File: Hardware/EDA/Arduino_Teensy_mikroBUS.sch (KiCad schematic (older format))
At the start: 30 parts, among them J1 HEADER_F_2.54MM_1R8P_ST_AU_PTH, J2 HEADER_F_2.54MM_1R8P_ST_AU_PTH, J3 HEADER_F_2.54MM_1R14P_ST_AU_P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, J4 HEADER_F_2.54MM_1R14P_ST_AU_P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, J5 Molex_0475710001, M1 FID, M2 FID, M3 FID, P1 HEADER_M_2.54MM_1R4P_ST_AU_PTH, P2 HEADER_M_2.54MM_1R4P_ST_AU_PTH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

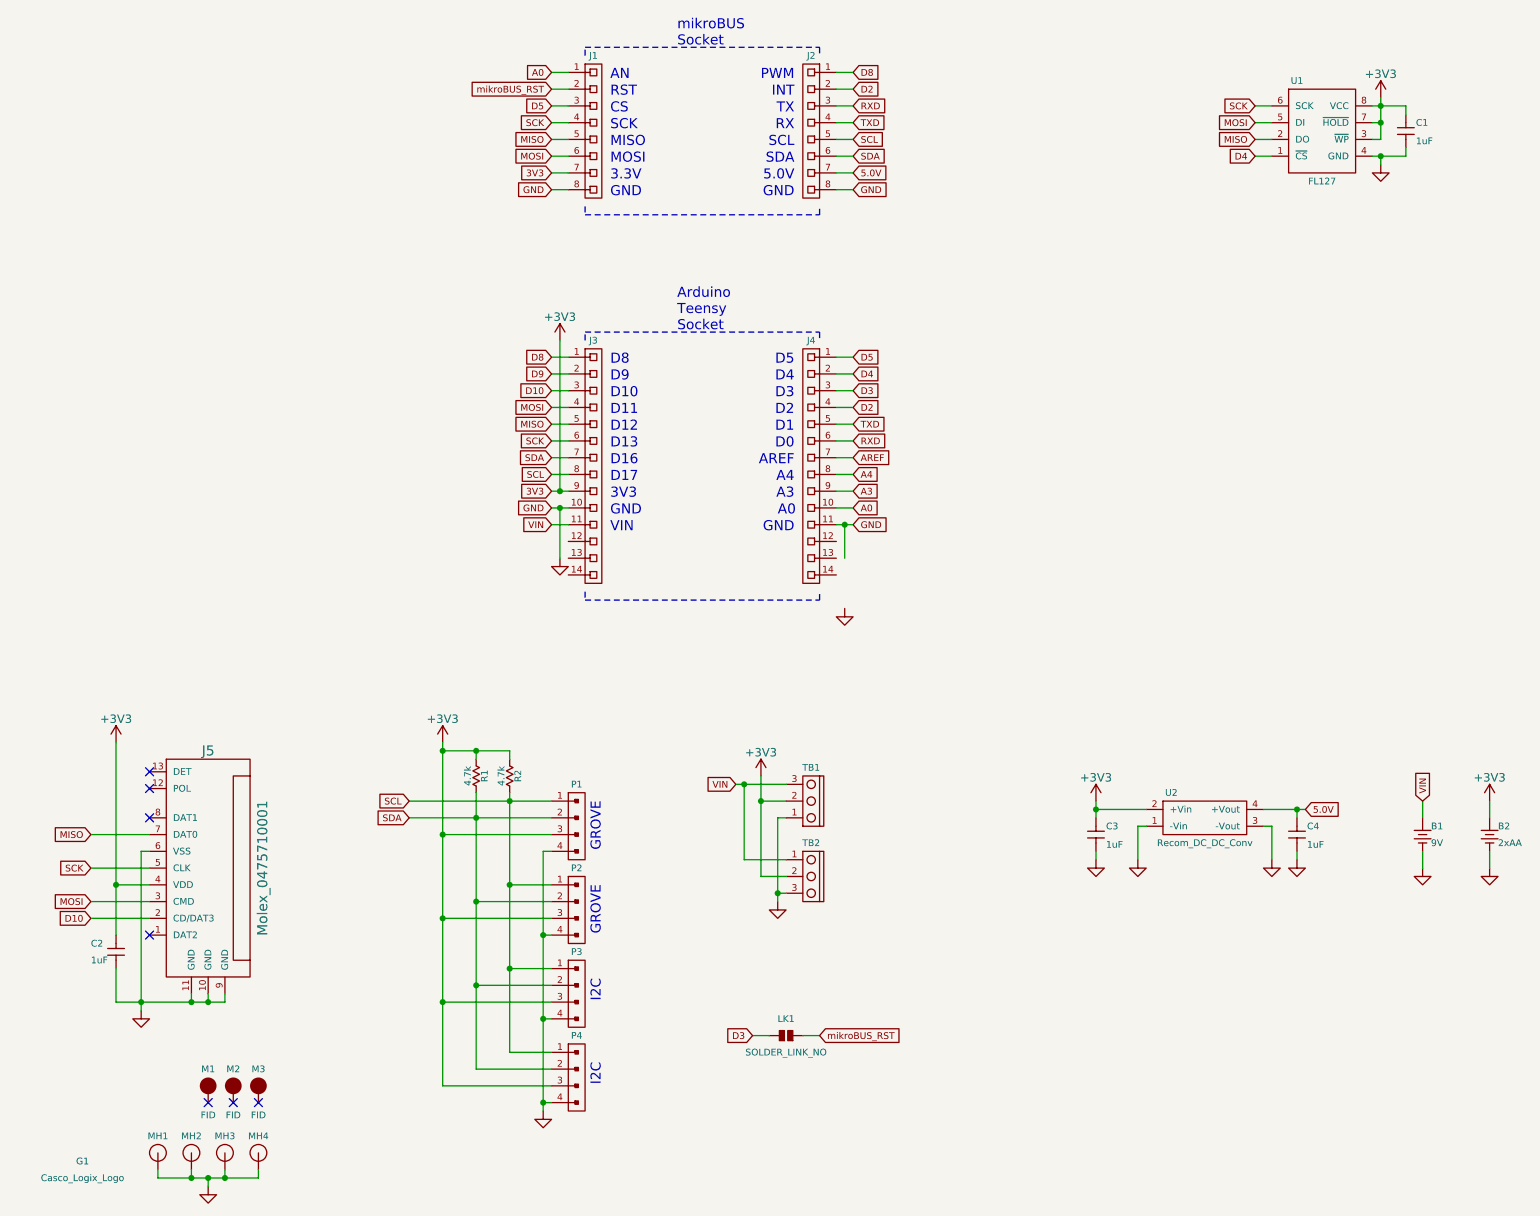
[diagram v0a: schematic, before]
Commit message: Updated schematic, netlist and read in netlist to PCB file.  Added pinouts for Teensy.
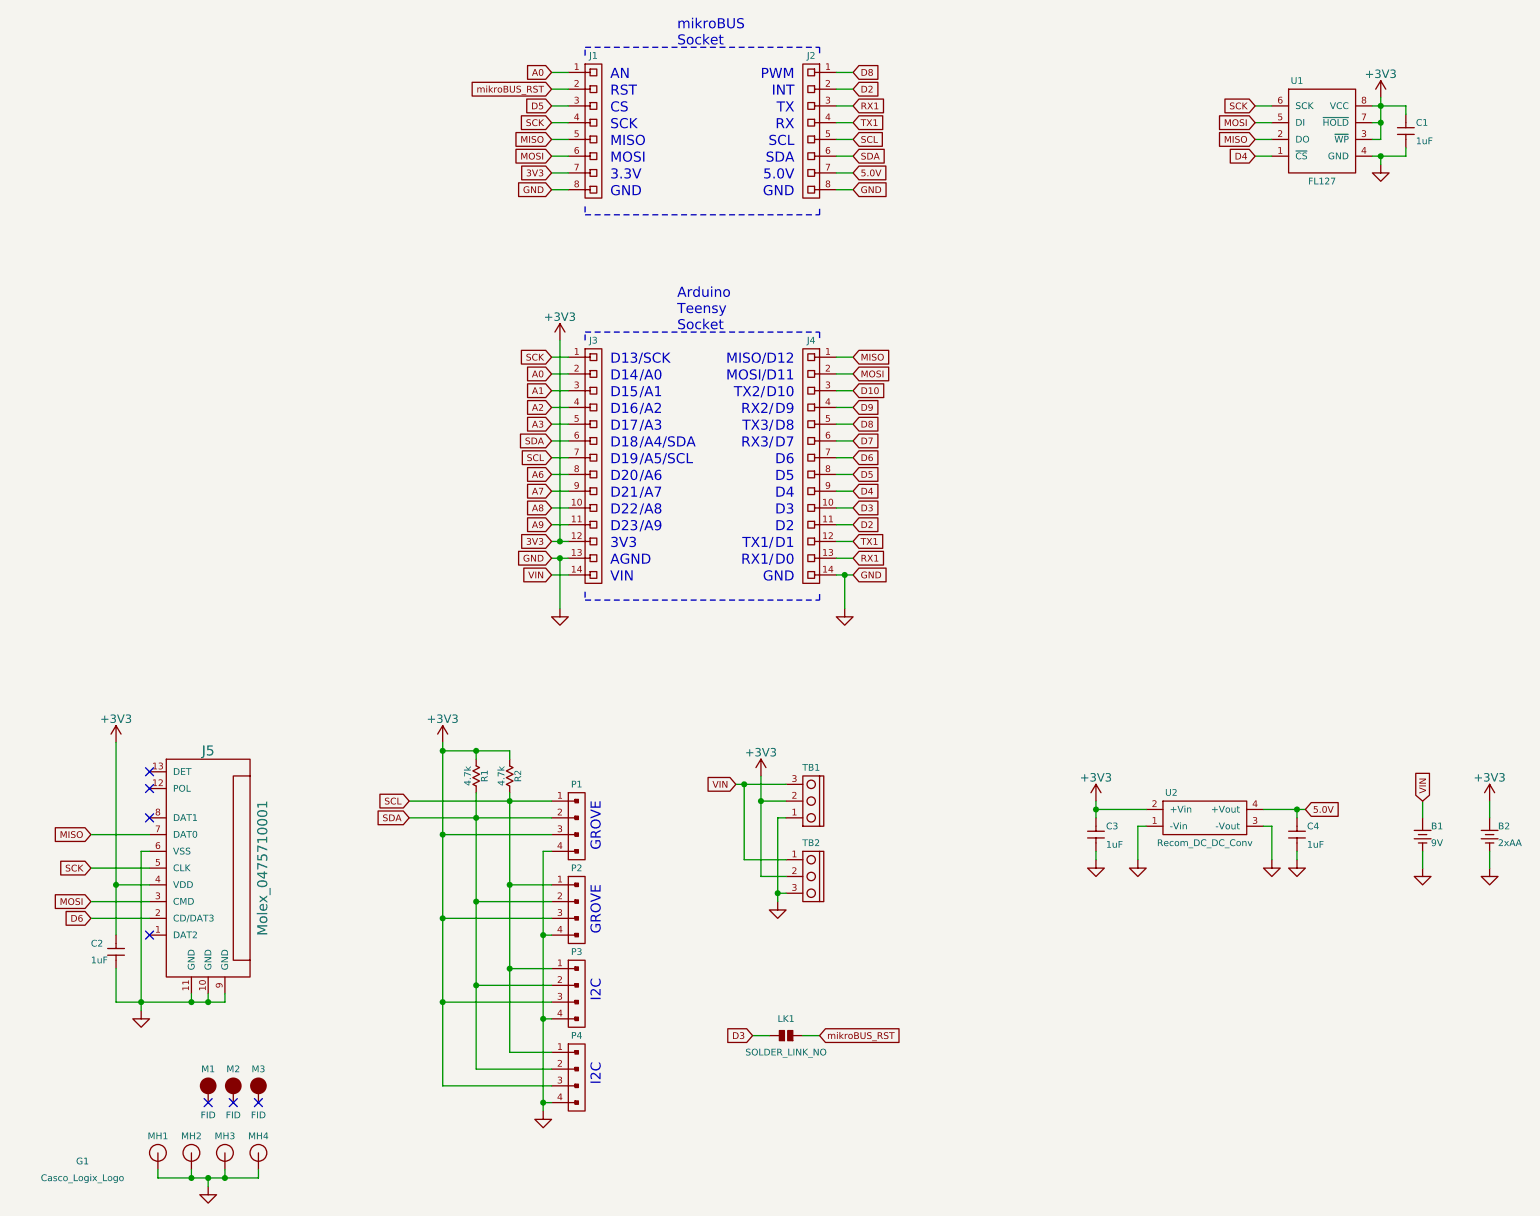
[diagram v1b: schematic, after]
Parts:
- B1: footprint (none) -> Battery:BC9VPC
- B2: footprint (none) -> Battery:Keystone_2462_2AA
- J3, J4: footprint (none) -> Header:HEADER_F_2.54MM_1R14P_ST_AU_PTH
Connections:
- net A4 is gone; now on net D5: J4.8 (P1)
- net +3V3: now also J3.12 (P1); no longer J3.9 (P1)
- net A0: now also J3.2 (P1); no longer J4.10 (P1)
- net A3: now also J3.5 (P1); no longer J4.9 (P1)
- net D10: now also J4.3 (P1); no longer J3.3 (P1), J5.2 (CD/DAT3)
- net D2: now also J4.11 (P1); no longer J4.4 (P1)
- net D3: now also J4.10 (P1); no longer J4.3 (P1)
- net D4: now also J4.9 (P1); no longer J4.2 (P1)
- net D5: no longer J4.1 (P1)
- net D8: now also J4.5 (P1); no longer J3.1 (P1)
- net D9: now also J4.4 (P1); no longer J3.2 (P1)
- net GND: now also J3.13 (P1), J4.14 (P1); no longer J3.10 (P1), J4.11 (P1)
- net MISO: now also J4.1 (P1); no longer J3.5 (P1)
- net MOSI: now also J4.2 (P1); no longer J3.4 (P1)
- net SCK: now also J3.1 (P1); no longer J3.6 (P1)
- net SCL: now also J3.7 (P1); no longer J3.8 (P1)
- net SDA: now also J3.6 (P1); no longer J3.7 (P1)
- net VIN: now also J3.14 (P1); no longer J3.11 (P1)
- net TX1: now reaches J4.12 (P1)
- net TX1: now also J2.4 (P1)
- net RX1: now reaches J4.13 (P1)
- net RX1: now also J2.3 (P1)
- net AREF renamed D6
- net D6: now also J5.2 (CD/DAT3)
- net RXD renamed D7
- net D7: no longer J2.3 (P1)
- removed net TXD: J2.4 (P1), J4.5 (P1)
- new net A1: J3.3 (P1)
- new net A2: J3.4 (P1)
- new net A6: J3.8 (P1)
- new net A7: J3.9 (P1)
- new net A8: J3.10 (P1)
- new net A9: J3.11 (P1)
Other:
- note added: "/A0"
- note added: "/A1"
- note added: "/A2"
- note added: "/A3"
- note added: "/A4/SDA"
- note added: "/A5/SCL"
- note added: "/A6"
- note added: "/A7"
- note added: "/A8"
- note added: "/A9"
- note added: "AGND"
- note added: "D13/SCK"
- note added: "D14"
- note added: "D15"
- note added: "D18"
- note added: "D19"
- note added: "D20"
- note added: "D21"
- note added: "D22"
- note added: "D23"
- note added: "D6"
- note added: "D7"
- note added: "MISO/D12"
- note added: "MOSI/D11"
- note added: "RX1/"
- note added: "RX2/"
- note added: "RX3/"
- note added: "TX1/"
- note added: "TX2/"
- note added: "TX3/"
- note removed: "A0"
- note removed: "A3"
- note removed: "A4"
- note removed: "AREF"
- note removed: "D11"
- note removed: "D12"
- note removed: "D13"

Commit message: Final changes prior to gerber verification.
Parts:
- U1: value FL127 -> FL116K
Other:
- moved on the sheet: LK1, M1, M2, M3, MH1, MH2, MH3, MH4, P1, P2, P3, P4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
